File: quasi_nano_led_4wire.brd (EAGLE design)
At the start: 32.7 x 52.1 mm, 4 parts, among them X1 JST-XH-02-PIN-LONG-PAD

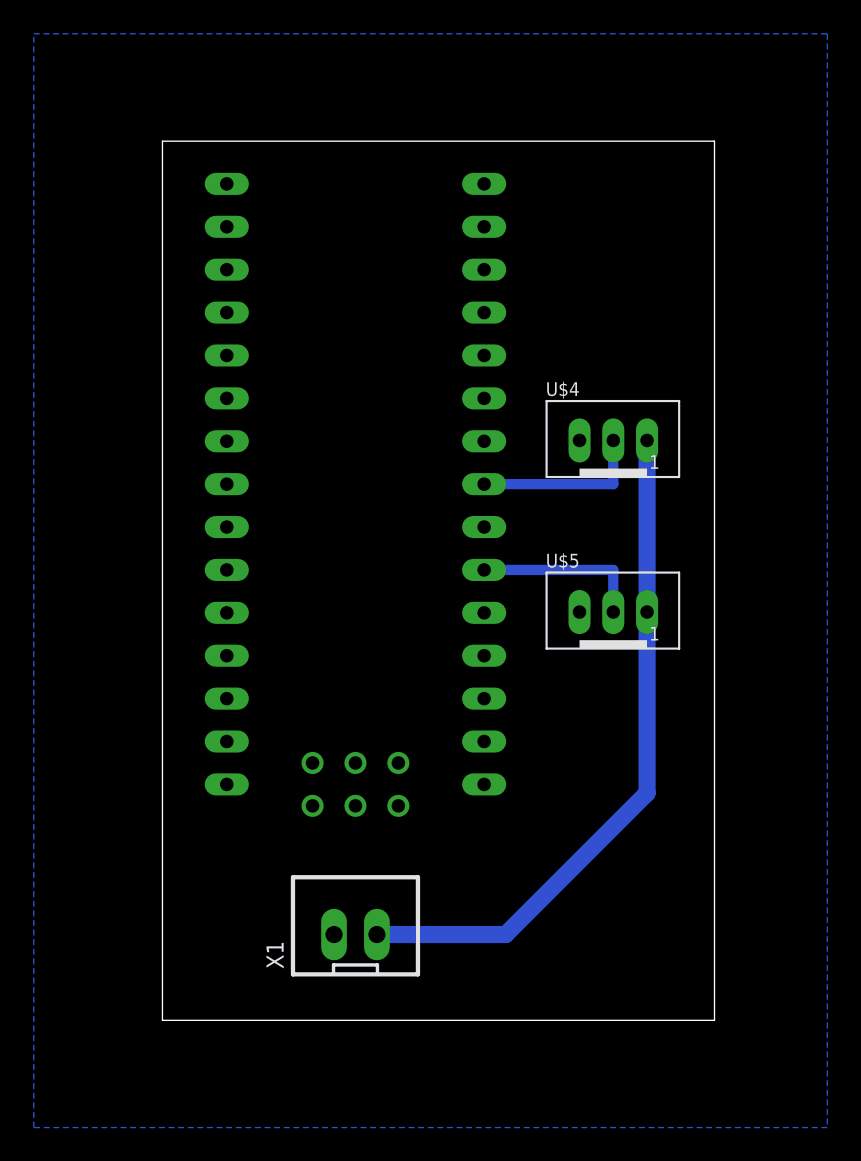
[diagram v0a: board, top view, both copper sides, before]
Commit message: add 4 wire board
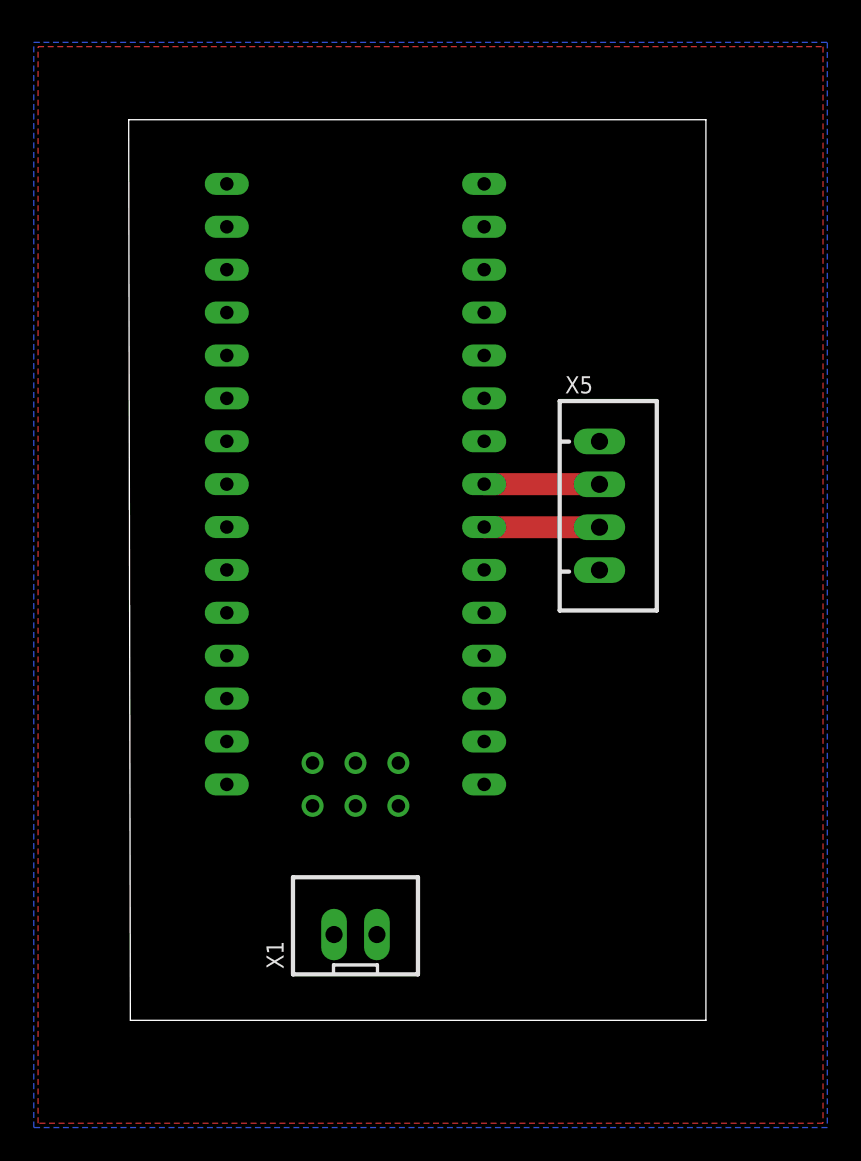
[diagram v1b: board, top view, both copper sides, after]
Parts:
- removed U$4, U$5: JST-PH_3-PIN_HEADER, con-jst-ph:JST_B3B-PH_HEADER
- added X5: JST-XH-04-PIN-LONG-PAD, Rembrandt Electronics - JST XH Connectors v1-0:JST-XH-04-PACKAGE-LONG-PAD
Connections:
- removed net N$4: U$4.P1, U$5.P1, X1.2
- removed net N$7: U$1.D3, U$5.P2
- new net 5V: X1.2, X5.1
- new net N$5: U$1.D5, X5.2
- net GND: now also X5.4; no longer U$4.P3, U$5.P3
- net N$6: now also U$1.D4, X5.3; no longer U$1.D5, U$4.P2
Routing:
- net N$4: track 40.3 -> 0.00 mm
- net N$7: track 10.1 -> 0.00 mm
- net N$5: track 0.00 -> 6.83 mm
- net N$6: track 10.2 -> 6.83 mm
- added copper zone on layer 1, net 5V
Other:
- board size 32.7 x 52.1 mm -> 34.2 x 53.3 mm
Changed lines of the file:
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@@
 <setting verticaltext="up"/>
 </settings>
-<grid distance="50" unitdist="mil" unit="mil" style="lines" multiple="1" display="no" altdistance="5" altunitdist="mil" altunit="mil"/>
+<grid distance="0.1" unitdist="mm" unit="mm" style="lines" multiple="10" display="yes" altdistance="5" altunitdist="mil" altunit="mm"/>
 <layers>
 <layer number="1" name="Top" color="4" fill="1" visible="yes" active="yes"/>
@@
 <board>
 <plain>
-<wire x1="7.62" y1="24.13" x2="40.31" y2="24.13" width="0" layer="20"/>
-<wire x1="40.31" y1="24.13" x2="40.31" y2="76.19" width="0" layer="20"/>
-<wire x1="40.31" y1="76.19" x2="7.62" y2="76.19" width="0" layer="20"/>
-<wire x1="7.62" y1="76.19" x2="7.62" y2="24.13" width="0" layer="20"/>
+<wire x1="5.72" y1="24.13" x2="39.802" y2="24.13" width="0" layer="20"/>
+<wire x1="39.802" y1="24.13" x2="39.802" y2="77.46" width="0" layer="20"/>
+<wire x1="39.802" y1="77.46" x2="5.62" y2="77.46" width="0" layer="20"/>
+<wire x1="5.62" y1="77.46" x2="5.72" y2="24.13" width="0" layer="20"/>
 </plain>
 <attributes>
@@
 <elements>
 <element name="U$1" library="Arduino-clone" package="NANO" value="NANO" x="21.59" y="46.99" smashed="yes"/>
-<element name="U$4" library="con-jst-ph" package="JST_B3B-PH_HEADER" value="JST-PH_3-PIN_HEADER" x="34.29" y="58.42" smashed="yes">
-<attribute name="NAME" x="30.3175" y="61.1025" size="0.8128" layer="25" font="vector"/>
-</element>
-<element name="U$5" library="con-jst-ph" package="JST_B3B-PH_HEADER" value="JST-PH_3-PIN_HEADER" x="34.29" y="48.26" smashed="yes">
-<attribute name="NAME" x="30.3175" y="50.9425" size="0.8128" layer="25" font="vector"/>
-</element>
 <element name="X1" library="Rembrandt Electronics - JST XH Connectors v1-0" package="JST-XH-02-PACKAGE-LONG-PAD" value="JST-XH-02-PIN-LONG-PAD" x="19.05" y="29.21" smashed="yes">
 <attribute name="NAME" x="14.795" y="27.17" size="1.016" layer="25" ratio="10" rot="R90"/>
 <attribute name="VALUE" x="15.7475" y="33.1025" size="1.016" layer="27" ratio="10"/>
 </element>
+<element name="X5" library="Rembrandt Electronics - JST XH Connectors v1-0" package="JST-XH-04-PACKAGE-LONG-PAD" value="JST-XH-04-PIN-LONG-PAD" x="33.5" y="54.6" smashed="yes" rot="R270">
+<attribute name="NAME" x="31.46" y="61.255" size="1.016" layer="25" ratio="10"/>
+<attribute name="VALUE" x="37.3925" y="60.6025" size="1.016" layer="27" ratio="10" rot="R270"/>
+</element>
 </elements>
 <signals>
-<signal name="N$4">
-<contactref element="U$4" pad="P1"/>
-<contactref element="U$5" pad="P1"/>
-<contactref element="X1" pad="2"/>
-<wire x1="36.3175" y1="58.4675" x2="36.3175" y2="48.3075" width="1.016" layer="16"/>
-<wire x1="36.3175" y1="37.5875" x2="27.94" y2="29.21" width="1.016" layer="16"/>
-<wire x1="27.94" y1="29.21" x2="20.32" y2="29.21" width="1.016" layer="16"/>
-<wire x1="36.3175" y1="48.3075" x2="36.3175" y2="37.5875" width="1.016" layer="16"/>
-</signal>
-<signal name="N$6">
-<contactref element="U$4" pad="P2"/>
-<contactref element="U$1" pad="D5"/>
-<wire x1="26.67" y1="55.88" x2="34.3175" y2="55.88" width="0.6096" layer="16"/>
-<wire x1="34.3175" y1="55.88" x2="34.3175" y2="58.4675" width="0.6096" layer="16"/>
-</signal>
-<signal name="N$7">
-<contactref element="U$1" pad="D3"/>
-<contactref element="U$5" pad="P2"/>
-<wire x1="34.3175" y1="48.3075" x2="34.3175" y2="50.8" width="0.6096" layer="16"/>
-<wire x1="34.3175" y1="50.8" x2="26.67" y2="50.8" width="0.6096" layer="16"/>
-</signal>
 <signal name="GND">
 <polygon width="0.1524" layer="16" isolate="0.8128">
-<vertex x="0" y="82.55"/>
-<vertex x="46.99" y="82.55"/>
+<vertex x="0" y="82.042"/>
+<vertex x="46.99" y="82.042"/>
 <vertex x="46.99" y="17.78"/>
 <vertex x="0" y="17.78"/>
@@
 <contactref element="X1" pad="1"/>
 <contactref element="U$1" pad="GND"/>
-<contactref element="U$5" pad="P3"/>
-<contactref element="U$4" pad="P3"/>
 <contactref element="U$1" pad="GND1"/>
+<contactref element="X5" pad="4"/>
+<wire x1="11.43" y1="40.64" x2="26.67" y2="45.72" width="0" layer="19" extent="1-1"/>
+<wire x1="17.78" y1="29.21" x2="11.43" y2="40.64" width="0" layer="19" extent="1-1"/>
+<wire x1="33.5" y1="50.79" x2="17.78" y2="29.21" width="0" layer="19" extent="1-1"/>
+</signal>
+<signal name="5V">
+<contactref element="X1" pad="2"/>
+<polygon width="0.1524" layer="1" isolate="0.8128">
+<vertex x="0.254" y="18.034"/>
+<vertex x="0.254" y="81.788"/>
+<vertex x="46.736" y="81.788"/>
+<vertex x="46.736" y="18.034"/>
+</polygon>
+<contactref element="X5" pad="1"/>
+<wire x1="33.5" y1="58.41" x2="20.32" y2="29.21" width="0" layer="19" extent="1-1"/>
+</signal>
+<signal name="N$5">
+<contactref element="U$1" pad="D5"/>
+<contactref element="X5" pad="2"/>
+<wire x1="26.67" y1="55.88" x2="33.49" y2="55.88" width="1.3" layer="1"/>
+<wire x1="33.49" y1="55.88" x2="33.5" y2="55.87" width="1.3" layer="1"/>
+</signal>
+<signal name="N$6">
+<contactref element="X5" pad="3"/>
+<contactref element="U$1" pad="D4"/>
+<wire x1="33.5" y1="53.33" x2="26.68" y2="53.33" width="1.3" layer="1"/>
+<wire x1="26.68" y1="53.33" x2="26.67" y2="53.34" width="1.3" layer="1"/>
 </signal>
 </signals>
